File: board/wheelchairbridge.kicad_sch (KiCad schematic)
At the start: 54 parts, among them J1 male-joystick in, J10 grove-I2C-2, J2 female-to wheelchair, J3 12V, J4 AlarmIn1, J5 AlarmIn2, J6 grove-Serial, J7 grove-I2C, J8 grove-I2C-2, J9 grove-I2C, K1 RTE2xxxx, M1 Module_RaspberryPi_PicoW_Sock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, Q2 BC850, U1 LM7805_TO220, U2 AD5282, U3 TIL111, U4 TIL111

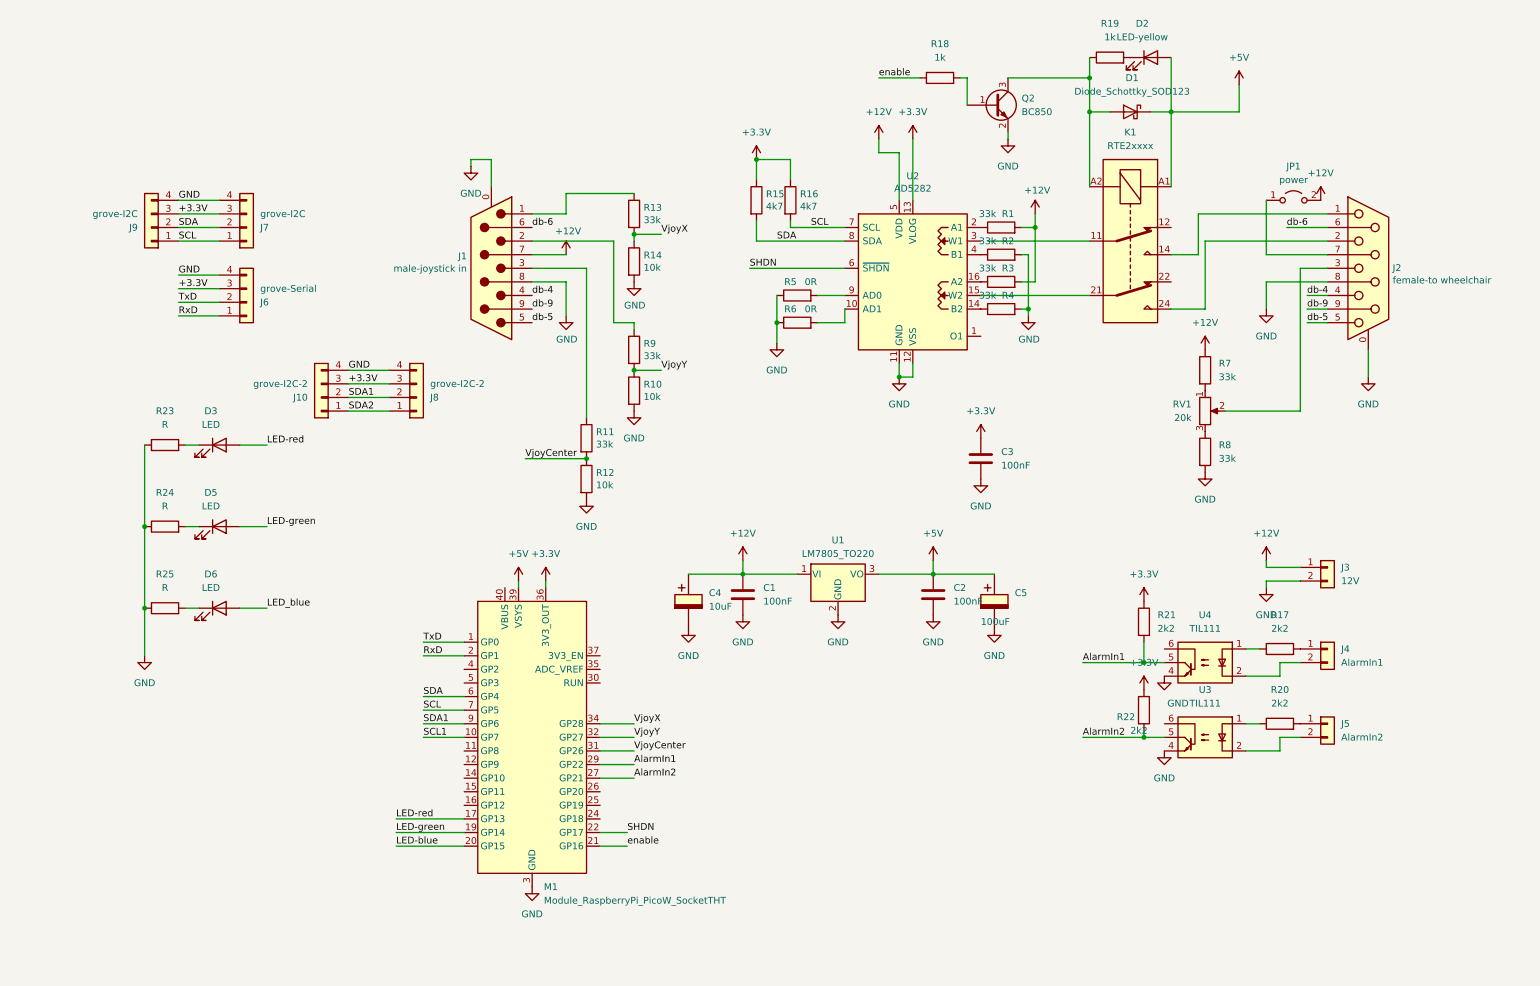
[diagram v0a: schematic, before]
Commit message: Added Solid State relays for low-power signal switching. Switch from edge to regular DB9 connectors Refactored schematic PCB layout
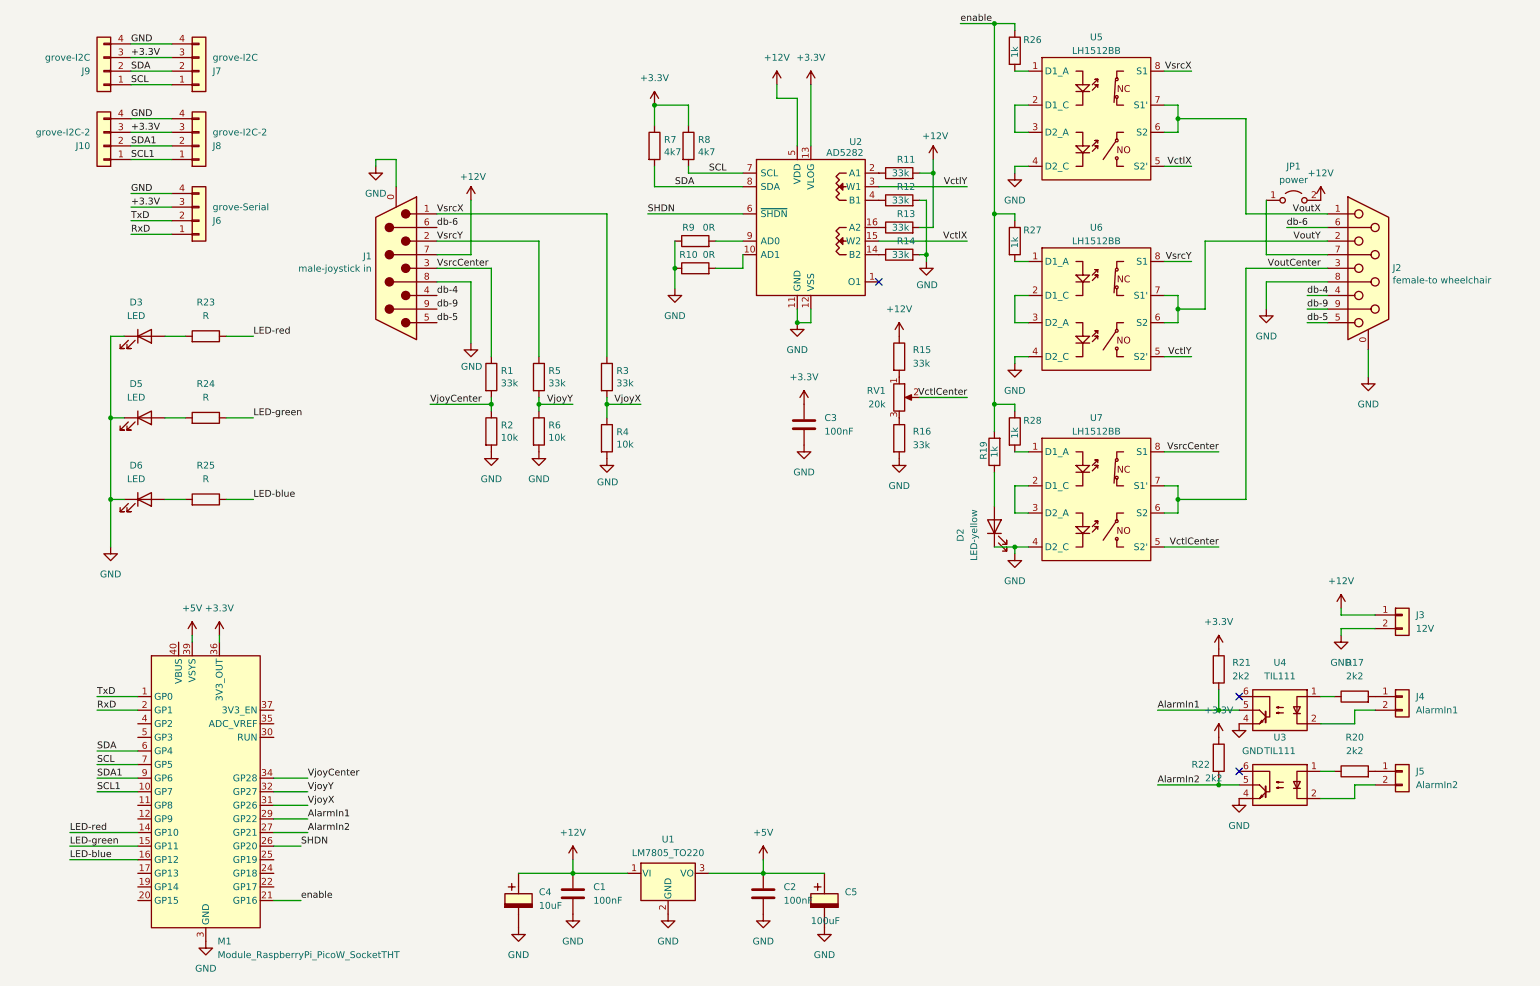
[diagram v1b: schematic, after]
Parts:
- removed D1: Diode_Schottky_SOD123, fab:SOD-123, symbol fab:Diode_Schottky_SOD123
- removed K1: RTE2xxxx, Relay_THT:Relay_DPDT_Schrack-RT2-FormC_RM5mm, symbol Relay:RTE2xxxx
- removed Q2: BC850, Package_TO_SOT_SMD:SOT-23, symbol Transistor_BJT:BC850
- removed R18: 1k, Resistor_SMD:R_0805_2012Metric, symbol Device:R
- added R26, R27, R28: 1k, Resistor_SMD:R_0805_2012Metric, symbol Device:R
- added U5, U6, U7: LH1512BB, Package_DIP:DIP-8_W7.62mm_Socket_LongPads, symbol parts:LH1512BB
- J1: footprint Connector_Dsub:DSUB-9_Male_Horizontal_P2.77x2.84mm_EdgePinOffset4.94mm_Housed_MountingHolesOffset7.48mm -> Connector_Dsub:DSUB-9_Pins_Horizontal_P2.77x2.84mm_EdgePinOffset4.94mm_Housed_MountingHolesOffset4.94mm
- J2: footprint Connector_Dsub:DSUB-9_Female_Horizontal_P2.77x2.84mm_EdgePinOffset4.94mm_Housed_MountingHolesOffset7.48mm -> Connector_Dsub:DSUB-9_Socket_Horizontal_P2.77x2.84mm_EdgePinOffset4.94mm_Housed_MountingHolesOffset4.94mm
- R25: footprint LED_SMD:LED_1206_3216Metric_Pad1.42x1.75mm_HandSolder -> Resistor_SMD:R_0805_2012Metric
- renumbered R11 to R1, R6 to R10, R1 to R11, R2 to R12, R3 to R13, R4 to R14, R7 to R15, R8 to R16, R12 to R2, R13 to R3, R14 to R4, R9 to R5, R10 to R6, R15 to R7, R16 to R8, R5 to R9
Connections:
- net LED_blue is gone; now on an unnamed net: D6.2 (A)
- net SDA2 is gone; now on net SCL1: J10.1 (Pin_1), J8.1 (Pin_1)
- net +5V: no longer D2.2 (A)
- net GND: now also D2.1 (K), D3.1 (K), D5.1 (K), D6.1 (K), U5.4 (D2_C), U6.4 (D2_C), U7.4 (D2_C); no longer R23.1, R24.1, R25.1
- net LED-blue: now also M1.16 (GP12), R25.1; no longer M1.20 (GP15)
- net LED-green: now also M1.15 (GP11), R24.1; no longer D5.2 (A), M1.19 (GP14)
- net LED-red: now also M1.14 (GP10), R23.1; no longer D3.2 (A), M1.17 (GP13)
- net SHDN: now also M1.26 (GP20); no longer M1.22 (GP17)
- net VjoyCenter: now also M1.34 (GP28); no longer M1.31 (GP26)
- net VjoyX: now also M1.31 (GP26); no longer M1.34 (GP28)
- net enable: now also R19.2, R26.1, R27.1, R28.1
- net at R19.1: now also D2.2 (A)
- net at R23.2: now also D3.2 (A); no longer D3.1 (K)
- net at R25.2: no longer D6.1 (K)
- net at R24.2: now also D5.2 (A); no longer D5.1 (K)
- net VsrcX: now reaches J1.1, R3.1
- net VsrcX: now also U5.8 (S1)
- net VctlX: now reaches U2.15 (W2)
- net VctlX: now also U5.5 (S2')
- net VctlY: now reaches U2.3 (W1)
- net VctlY: now also U6.5 (S2')
- net VctlCenter: now reaches RV1.2
- net VctlCenter: now also U7.5 (S2'); no longer J2.3
- net VsrcY: now reaches J1.2, R5.1
- net VsrcY: now also U6.8 (S1)
- net VsrcCenter: now reaches J1.3, R1.1
- net VsrcCenter: now also U7.8 (S1)
- net VoutX: now reaches J2.1
- net VoutX: now also U5.6 (S2), U5.7 (S1')
- net VoutY: now reaches J2.2
- net VoutY: now also U6.6 (S2), U6.7 (S1')
- new net: R26.2, U5.1 (D1_A)
- new net: U5.2 (D1_C), U5.3 (D2_A)
- new net: R27.2, U6.1 (D1_A)
- new net: U6.2 (D1_C), U6.3 (D2_A)
- new net: R28.2, U7.1 (D1_A)
- new net: U7.2 (D1_C), U7.3 (D2_A)
- new net VoutCenter: J2.3, U7.6 (S2), U7.7 (S1')
- no-connect marks 0 -> 3
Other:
- moved on the sheet: C1, C2, C3, C4, C5, D2, D3, D5, D6, J1, J10, J3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

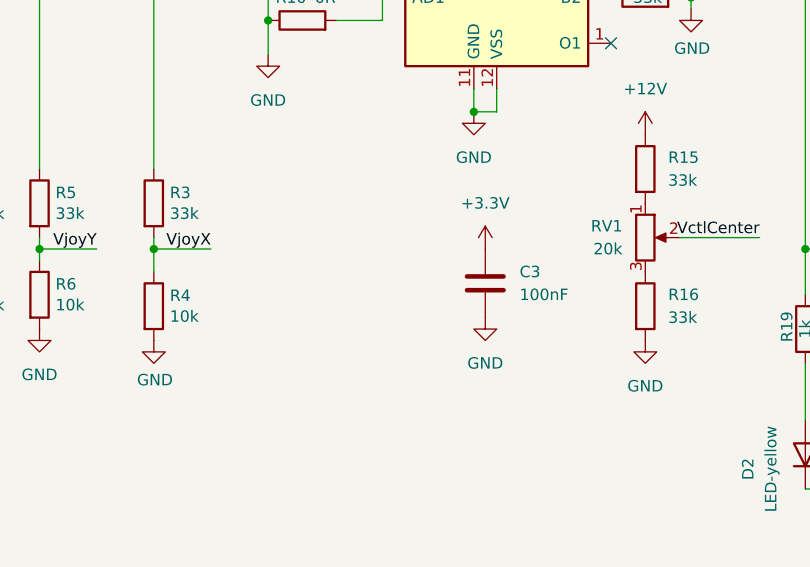
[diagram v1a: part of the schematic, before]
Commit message: Alarm labels were wrong Added 100nF cap on 12V for digipot
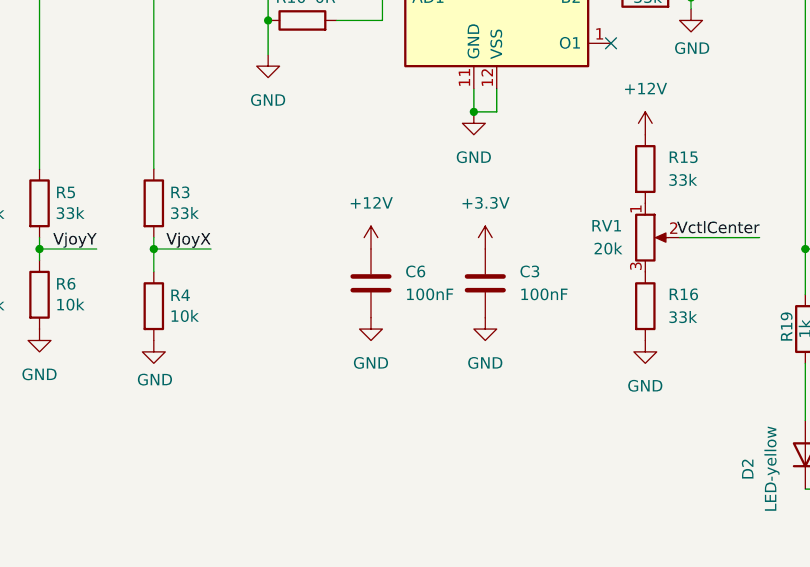
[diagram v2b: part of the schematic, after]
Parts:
- added C6: 100nF, Capacitor_SMD:C_1206_3216Metric, symbol Device:C
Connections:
- net +12V: now also C6.1
- net GND: now also C6.2
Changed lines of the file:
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@@
 	)
 	(symbol
+		(lib_id "power:+12V")
+		(at 146.05 85.09 0)
+		(unit 1)
+		(exclude_from_sim no)
+		(in_bom yes)
+		(on_board yes)
+		(dnp no)
+		(fields_autoplaced yes)
+		(property "Reference" "#PWR020"
+			(at 146.05 88.9 0)
+			(effects
+				(font
+					(size 1.27 1.27)
+				)
+				(hide yes)
+			)
+		)
+		(property "Value" "+12V"
+			(at 146.05 80.01 0)
+			(effects
+				(font
+					(size 1.27 1.27)
+				)
+			)
+		)
+		(property "Footprint" ""
+			(at 146.05 85.09 0)
+			(effects
+				(font
+					(size 1.27 1.27)
+				)
+				(hide yes)
+			)
+		)
+		(property "Datasheet" ""
+			(at 146.05 85.09 0)
+			(effects
+				(font
+					(size 1.27 1.27)
+				)
+				(hide yes)
+			)
+		)
+		(property "Description" ""
+			(at 146.05 85.09 0)
+			(effects
+				(font
+					(size 1.27 1.27)
+				)
+			)
+		)
+		(pin "1"
+		)
+		(instances
+			(project "wheelchairbridge"
+				(path "/625d6cbe-11aa-45cc-bc83-c7f06504afa6"
+					(reference "#PWR020")
+					(unit 1)
+				)
+			)
+		)
+	)
+	(symbol
 		(lib_id "power:GND")
 		(at 240.03 144.78 0)
@@
 	)
 	(symbol
+		(lib_id "Device:C")
+		(at 146.05 88.9 0)
+		(unit 1)
+		(exclude_from_sim no)
+		(in_bom yes)
+		(on_board yes)
+		(dnp no)
+		(fields_autoplaced yes)
+		(property "Reference" "C6"
+			(at 149.86 87.63 0)
+			(effects
+				(font
+					(size 1.27 1.27)
+				)
+				(justify left)
+			)
+		)
+		(property "Value" "100nF"
+			(at 149.86 90.17 0)
+			(effects
+				(font
+					(size 1.27 1.27)
+				)
+				(justify left)
+			)
+		)
+		(property "Footprint" "Capacitor_SMD:C_1206_3216Metric"
+			(at 147.0152 92.71 0)
+			(effects
+				(font
+					(size 1.27 1.27)
+				)
+				(hide yes)
+			)
+		)
+		(property "Datasheet" "~"
+			(at 146.05 88.9 0)
+			(effects
+				(font
+					(size 1.27 1.27)
+				)
+				(hide yes)
+			)
+		)
+		(property "Description" ""
+			(at 146.05 88.9 0)
+			(effects
+				(font
+					(size 1.27 1.27)
+				)
+			)
+		)
+		(pin "1"
+		)
+		(pin "2"
+		)
+		(instances
+			(project "wheelchairbridge"
+				(path "/625d6cbe-11aa-45cc-bc83-c7f06504afa6"
+					(reference "C6")
+					(unit 1)
+				)
+			)
+		)
+	)
+	(symbol
 		(lib_id "Device:R")
 		(at 46.99 102.87 270)
@@
 					(unit 1)
 				)
+			)
+		)
+	)
+	(symbol
+		(lib_id "power:GND")
+		(at 146.05 92.71 0)
+		(unit 1)
+		(exclude_from_sim no)
+		(in_bom yes)
+		(on_board yes)
+		(dnp no)
+		(fields_autoplaced yes)
+		(property "Reference" "#PWR044"
+			(at 146.05 99.06 0)
+			(effects
+				(font
+					(size 1.27 1.27)
+				)
+				(hide yes)
+			)
+		)
+		(property "Value" "GND"
+			(at 146.05 97.79 0)
+			(effects
+				(font
+					(size 1.27 1.27)
+				)
+			)
+		)
+		(property "Footprint" ""
+			(at 146.05 92.71 0)
+			(effects
+				(font
+					(size 1.27 1.27)
+				)
+				(hide yes)
+			)
+		)
+		(property "Datasheet" ""
+			(at 146.05 92.71 0)
+			(effects
+				(font
+					(size 1.27 1.27)
+				)
+				(hide yes)
+			)
+		)
+		(property "Description" ""
+			(at 146.05 92.71 0)
+			(effects
+				(font
+					(size 1.27 1.27)
+				)
+			)
+		)
+		(pin "1"
+		)
+		(instances
+			(project "wheelchairbridge"
+				(path "/625d6cbe-11aa-45cc-bc83-c7f06504afa6"
+					(reference "#PWR044")
+					(unit 1)
+				)
